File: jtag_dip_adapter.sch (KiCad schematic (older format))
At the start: 22 parts, among them J1 USB_B_Micro, J2 Conn_01x22, J3 Conn_01x22, J4 JTAG, J5 Conn_01x02, U1 MAX40203AUK+T, U2 74LVC1G04

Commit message: initial layout
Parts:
- added D3: BAT54W, Package_TO_SOT_SMD:SOT-323_SC-70, symbol Diode:BAT54W
- D2: symbol THS-80-rescue:LED-Device-max_breakout-rescue-sbc_z80-rescue -> Device:LED
- J1: symbol max_breakout-rescue:USB_B_Micro-Connector -> jtag_dip_adapter-rescue:USB_B_Micro-Connector-max_breakout-rescue
- U1: symbol max_breakout-rescue:MAX40200AUK-Analog_Switch -> jtag_dip_adapter-rescue:MAX40200AUK-Analog_Switch-max_breakout-rescue
- U2: value 74LVC1G04 -> 74HCT1G04
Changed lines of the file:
@@
 TCK
-$Comp
-L THS-80-rescue:LED-Device-max_breakout-rescue-sbc_z80-rescue D2
-U 1 1 5DC12F86
-P 9600 5150
-AR Path="/5DC12F86" Ref="D2"  Part="1"
-AR Path="/5D70CA34/5DC12F86" Ref="D?"  Part="1"
-F 0 "D2" H 9625 5025 50  0000 C CNN
-F 1 "Red" H 9600 5250 32  0000 C CNN
-F 2 "LED_SMD:LED_0603_1608Metric_Pad1.05x0.95mm_HandSolder" H 9600 5150 50  0001 C CNN
-F 3 "~" H 9600 5150 50  0001 C CNN
-	1    9600 5150
-	-1   0    0    1
-$EndComp
 $Comp
 L Device:R_Small R?
@@
 AR Path="/5D9FA47F" Ref="U2"  Part="1"
 F 0 "U2" H 9175 5417 50  0000 C CNN
-F 1 "74LVC1G04" H 9175 5326 50  0000 C CNN
+F 1 "74HCT1G04" H 9175 5326 50  0000 C CNN
 F 2 "Package_SO:TSOP-5_1.65x3.05mm_P0.95mm" H 9200 5150 50  0001 C CNN
 F 3 "https://www.mouser.com/datasheet/2/916/74HC_HCT3G04-1319126.pdf" H 9200 5150 50  0001 C CNN
@@
 $EndComp
 $Comp
-L max_breakout-rescue:USB_B_Micro-Connector J?
+L jtag_dip_adapter-rescue:USB_B_Micro-Connector-max_breakout-rescue J?
 U 1 1 5CF77AF9
 P 1250 1150
@@
 $EndComp
 $Comp
-L max_breakout-rescue:MAX40200AUK-Analog_Switch U1
+L jtag_dip_adapter-rescue:MAX40200AUK-Analog_Switch-max_breakout-rescue U1
 U 1 1 5D37EDF6
 P 2550 1050
@@
 $EndComp
 Wire Wire Line
-	1150 2450 1750 2450
-Text Label 1425 2450 2    50   ~ 0
+	850  2450 1450 2450
+Text Label 1125 2450 2    50   ~ 0
 VCC
 Wire Wire Line
-	1150 2550 1750 2550
-Text Label 1425 2550 2    50   ~ 0
+	850  2550 1750 2550
+Text Label 1150 2550 2    50   ~ 0
 GND
+$Comp
+L Device:LED D2
+U 1 1 5DC12F86
+P 9600 5150
+AR Path="/5DC12F86" Ref="D2"  Part="1"
+AR Path="/5D70CA34/5DC12F86" Ref="D?"  Part="1"
+F 0 "D2" H 9625 5025 50  0000 C CNN
+F 1 "Red" H 9600 5250 32  0000 C CNN
+F 2 "LED_SMD:LED_0603_1608Metric_Pad1.05x0.95mm_HandSolder" H 9600 5150 50  0001 C CNN
+F 3 "~" H 9600 5150 50  0001 C CNN
+	1    9600 5150
+	-1   0    0    1
+$EndComp
+$Comp
+L Diode:BAT54W D3
+U 1 1 5DE90127
+P 1600 2450
+F 0 "D3" H 1600 2716 50  0000 C CNN
+F 1 "BAT54W" H 1600 2625 50  0000 C CNN
+F 2 "Package_TO_SOT_SMD:SOT-323_SC-70" H 1600 2275 50  0001 C CNN
+F 3 "https://assets.nexperia.com/documents/data-sheet/BAT54W_SER.pdf" H 1600 2450 50  0001 C CNN
+	1    1600 2450
+	1    0    0    -1
+$EndComp
 $EndSCHEMATC

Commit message: finished routing and silkscreen
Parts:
- J4: symbol Connector:AVR-JTAG-10 -> jtag_dip_adapter-rescue:AVR-JTAG-10-Connector
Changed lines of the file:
@@
 EESchema Schematic File Version 4
-LIBS:max_breakout-cache
+LIBS:jtag_dip_adapter-cache
 EELAYER 30 0
 EELAYER END
@@
 	2500 5350 2500 5300
 $Comp
-L Connector:AVR-JTAG-10 J?
+L jtag_dip_adapter-rescue:AVR-JTAG-10-Connector J?
 U 1 1 5DC12FA5
 P 7500 4500
@@
 L Connector_Generic:Conn_01x02 J5
 U 1 1 5DE7BBC0
-P 1950 2450
-F 0 "J5" H 2030 2442 50  0000 L CNN
-F 1 "Conn_01x02" H 2030 2351 50  0000 L CNN
-F 2 "Connector_PinHeader_2.54mm:PinHeader_1x02_P2.54mm_Horizontal" H 1950 2450 50  0001 C CNN
-F 3 "~" H 1950 2450 50  0001 C CNN
-	1    1950 2450
-	1    0    0    -1
-$EndComp
-Wire Wire Line
-	850  2450 1450 2450
-Text Label 1125 2450 2    50   ~ 0
-VCC
-Wire Wire Line
-	850  2550 1750 2550
-Text Label 1150 2550 2    50   ~ 0
-GND
+P 1950 2550
+F 0 "J5" H 2030 2542 50  0000 L CNN
+F 1 "Conn_01x02" H 2030 2451 50  0000 L CNN
+F 2 "Connector_PinHeader_2.54mm:PinHeader_1x02_P2.54mm_Horizontal" H 1950 2550 50  0001 C CNN
+F 3 "~" H 1950 2550 50  0001 C CNN
+	1    1950 2550
+	1    0    0    1
+$EndComp
 $Comp
 L Device:LED D2
@@
 	-1   0    0    1
 $EndComp
+Text Label 1150 2550 2    50   ~ 0
+GND
+Wire Wire Line
+	850  2550 1750 2550
 $Comp
 L Diode:BAT54W D3
@@
 	1    0    0    -1
 $EndComp
+Text Label 1125 2450 2    50   ~ 0
+VCC
+Wire Wire Line
+	850  2450 1450 2450
 $EndSCHEMATC

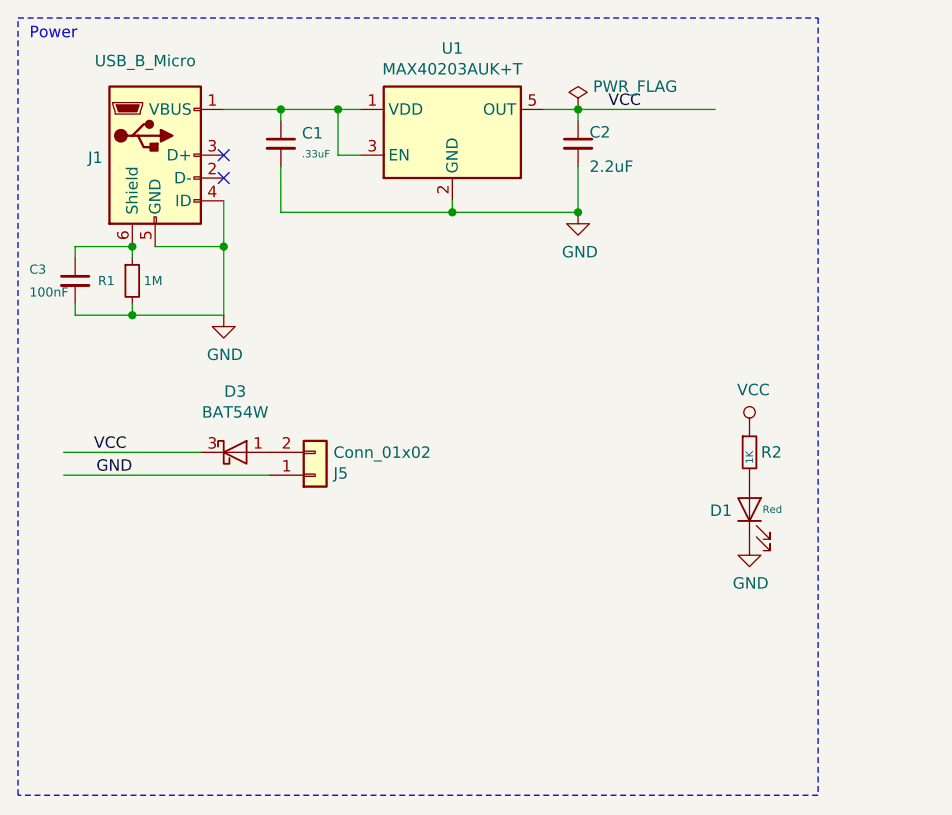
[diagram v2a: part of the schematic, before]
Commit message: added 5V ldo reg
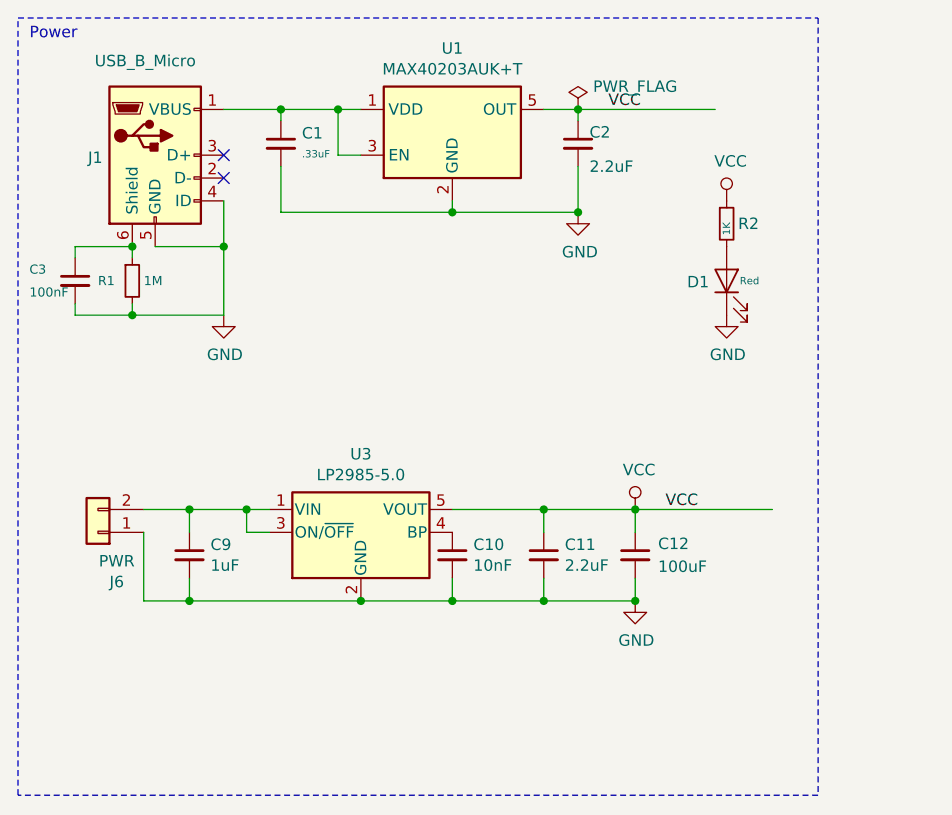
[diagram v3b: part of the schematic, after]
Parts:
- removed D3: BAT54W, Package_TO_SOT_SMD:SOT-323_SC-70, symbol Diode:BAT54W
- removed J5: Conn_01x02, Connector_PinHeader_2.54mm:PinHeader_1x02_P2.54mm_Horizontal, symbol Connector_Generic:Conn_01x02
- added C10: 10nF, Capacitor_SMD:C_0603_1608Metric_Pad1.05x0.95mm_HandSolder, symbol Device:C_Small
- added C11: 2.2uF, Capacitor_SMD:C_0603_1608Metric_Pad1.05x0.95mm_HandSolder, symbol Device:C_Small
- added C12: 100uF, Capacitor_SMD:C_1206_3216Metric_Pad1.42x1.75mm_HandSolder, symbol Device:C_Small
- added C9: 1uF, Capacitor_SMD:C_0603_1608Metric_Pad1.05x0.95mm_HandSolder, symbol Device:C_Small
- added J6: PWR, Connector_PinHeader_2.54mm:PinHeader_1x02_P2.54mm_Horizontal, symbol Connector_Generic:Conn_01x02
- added U3: LP2985-5.0, Package_TO_SOT_SMD:SOT-23-5, symbol Regulator_Linear:LP2985-5.0
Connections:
- wire segments 64 -> 83

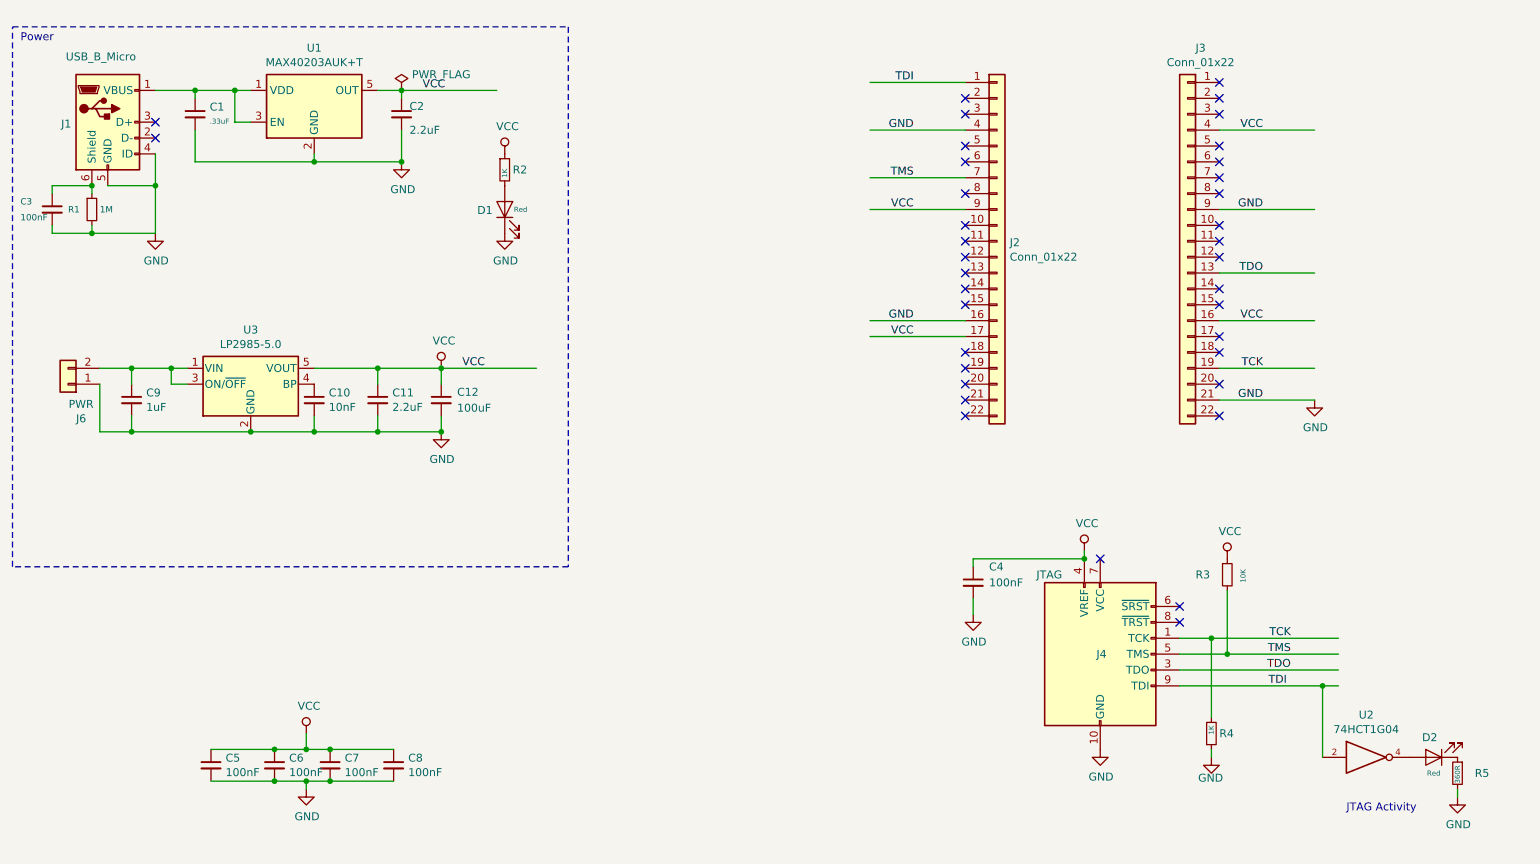
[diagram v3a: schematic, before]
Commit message: removed extra capacitor and vias
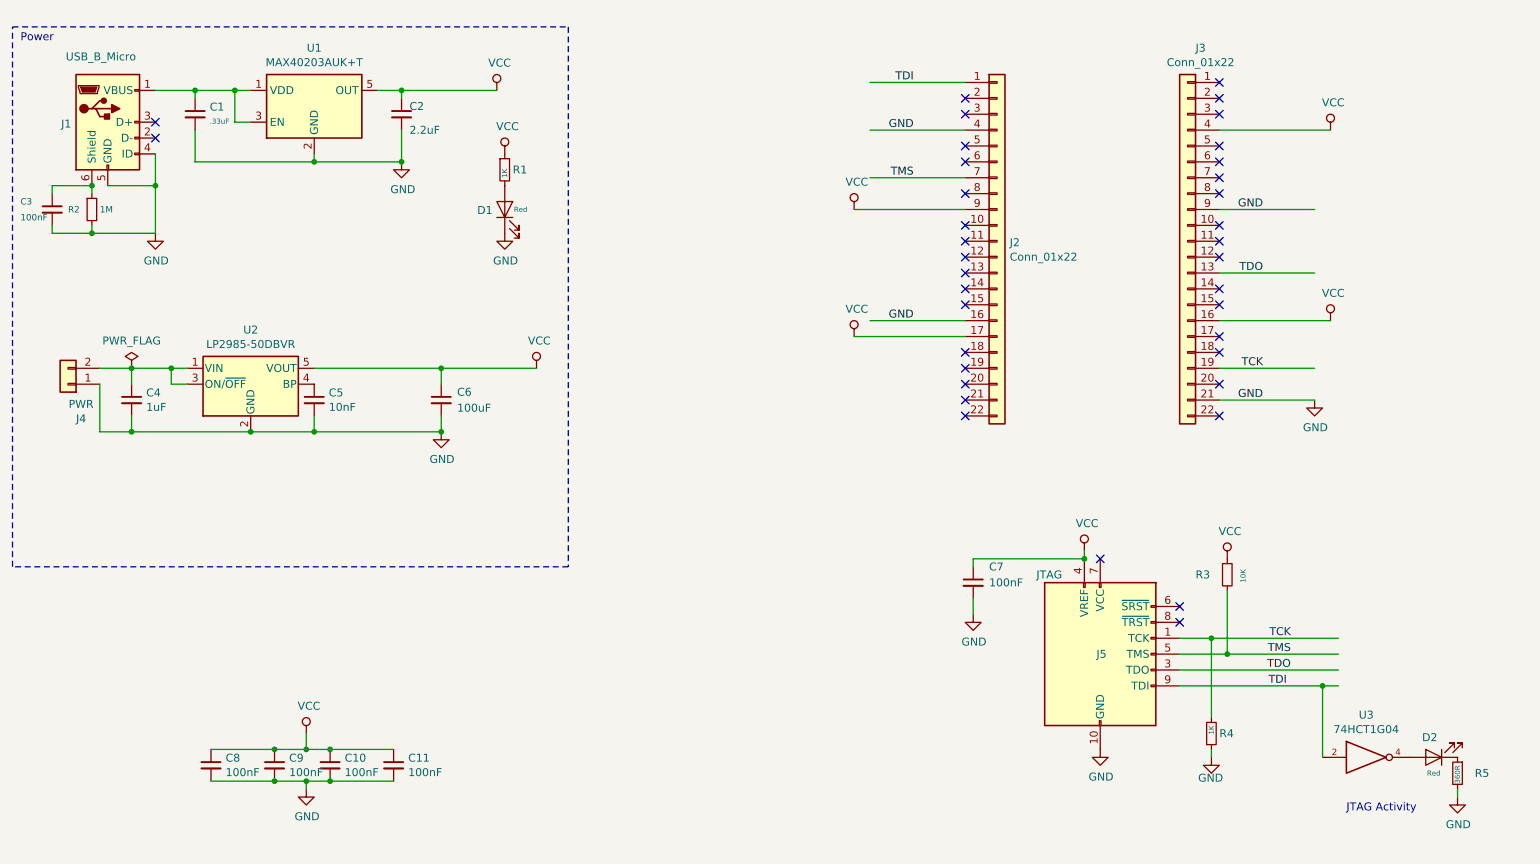
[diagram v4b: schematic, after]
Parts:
- removed C11: 2.2uF, Capacitor_SMD:C_0603_1608Metric_Pad1.05x0.95mm_HandSolder, symbol Device:C_Small
- U2: renamed from U3; value LP2985-5.0 -> LP2985-50DBVR; footprint Package_TO_SOT_SMD:SOT-23-5 -> Package_TO_SOT_SMD:SOT-23-5_HandSoldering
- renumbered C7 to C10, C8 to C11, C9 to C4, C10 to C5, C12 to C6, C4 to C7, C5 to C8, C6 to C9, J6 to J4, J4 to J5, R2 to R1, R1 to R2, U2 to U3
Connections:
- wire segments 83 -> 79
